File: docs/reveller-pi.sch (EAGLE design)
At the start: 12 parts, among them X1 332-26

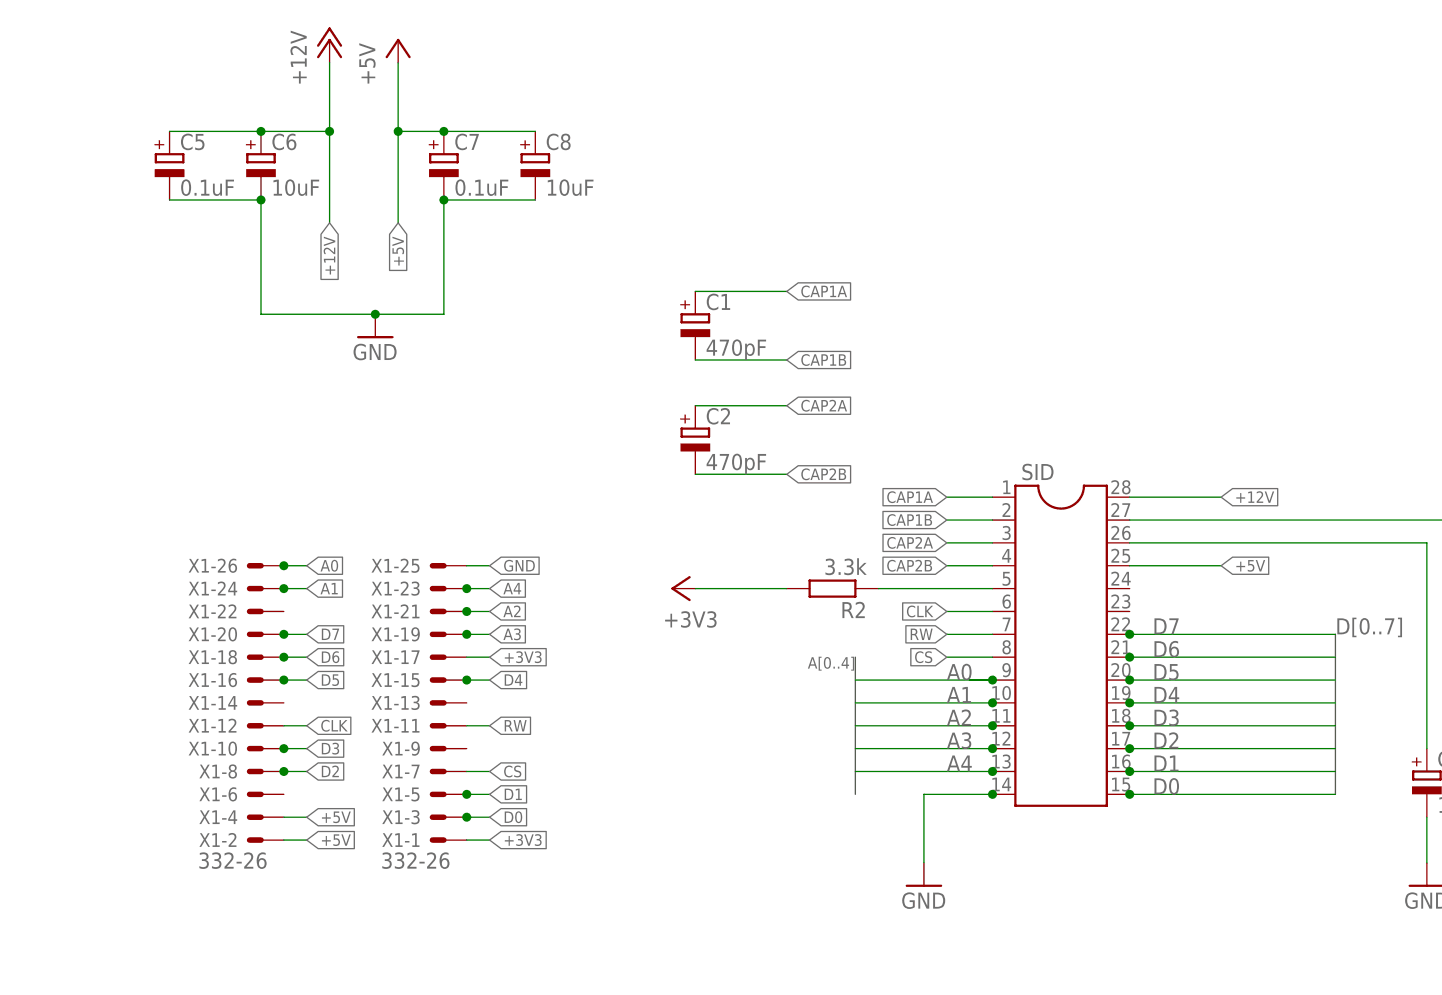
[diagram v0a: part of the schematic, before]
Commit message: updated schematics
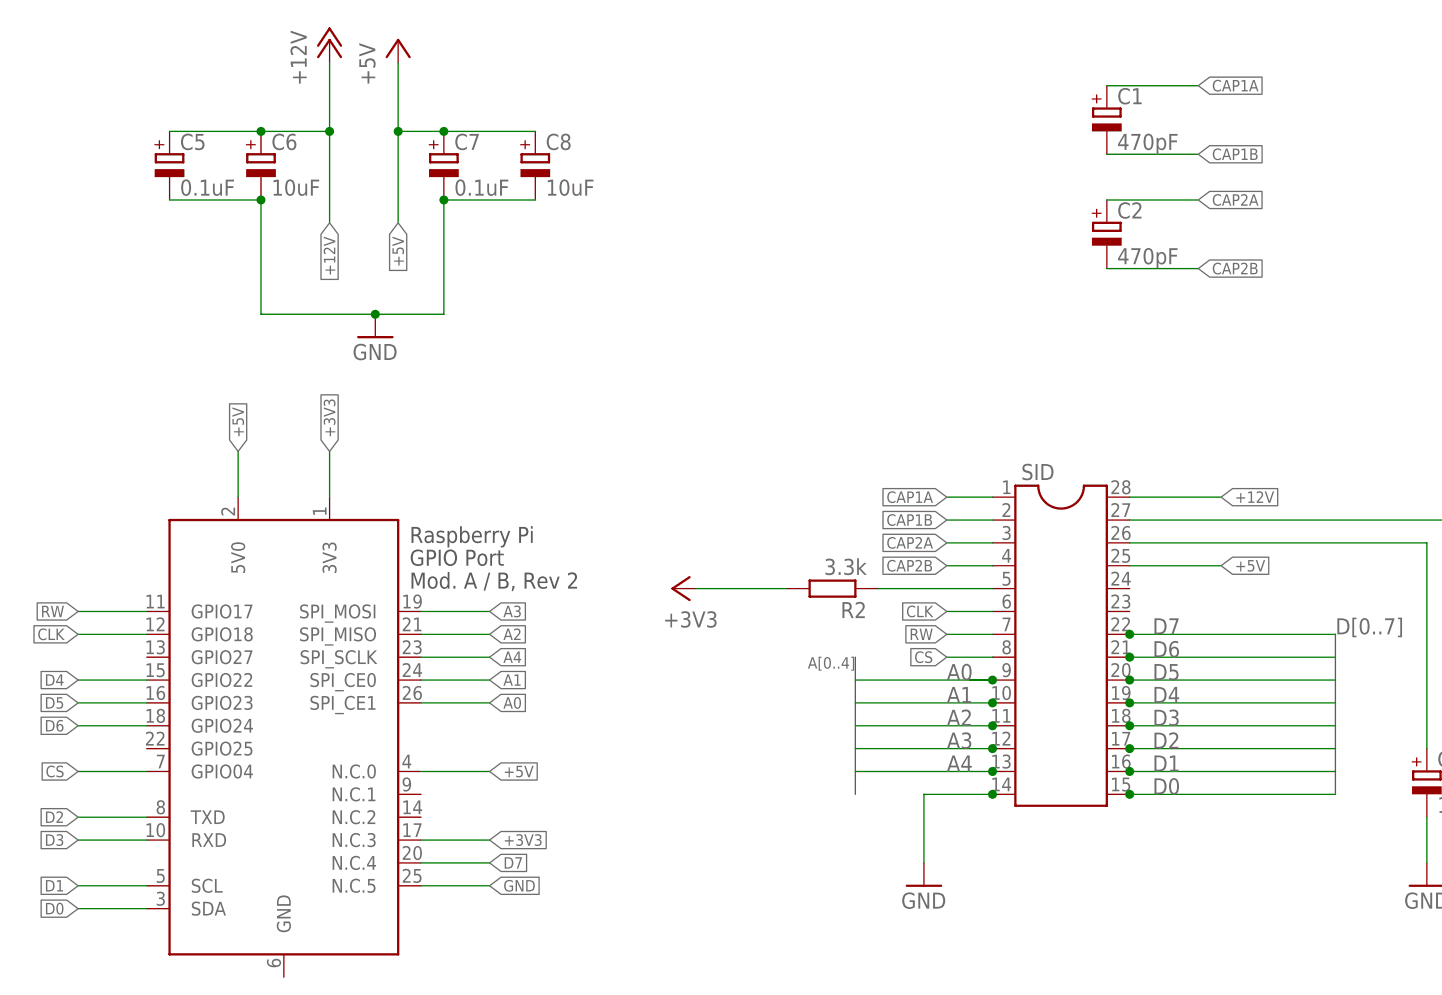
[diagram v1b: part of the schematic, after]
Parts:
- removed X1: 332-26, con-garry:332-26
- added X2: RASPI_BOARD_AB_E0, raspberrypi_bastelstube_v13:RASPI_BOARD_AB_E0
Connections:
- net +3V3: now also X2.3V3, X2.N.C.3; no longer X1-1.S, X1-17.S
- net +5V: now also X2.5V0, X2.N.C.0; no longer X1-2.S, X1-4.S
- net A0: now also X2.SPI_CE1; no longer X1-26.S
- net A1: now also X2.SPI_CE0; no longer X1-24.S
- net A2: now also X2.SPI_MISO; no longer X1-21.S
- net A3: now also X2.SPI_MOSI; no longer X1-19.S
- net A4: now also X2.SPI_SCLK; no longer X1-23.S
- net CLK: now also X2.GPIO18; no longer X1-12.S
- net CS: now also X2.GPIO04; no longer X1-7.S
- net D0: now also X2.SDA; no longer X1-3.S
- net D1: now also X2.SCL; no longer X1-5.S
- net D2: now also X2.TXD; no longer X1-8.S
- net D3: now also X2.RXD; no longer X1-10.S
- net D4: now also X2.GPIO22; no longer X1-15.S
- net D5: now also X2.GPIO23; no longer X1-16.S
- net D6: now also X2.GPIO24; no longer X1-18.S
- net D7: now also X2.N.C.4; no longer X1-20.S
- net GND: now also X2.N.C.5; no longer X1-25.S
- net RW: now also X2.GPIO17; no longer X1-11.S
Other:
- moved on the sheet: C1, C2

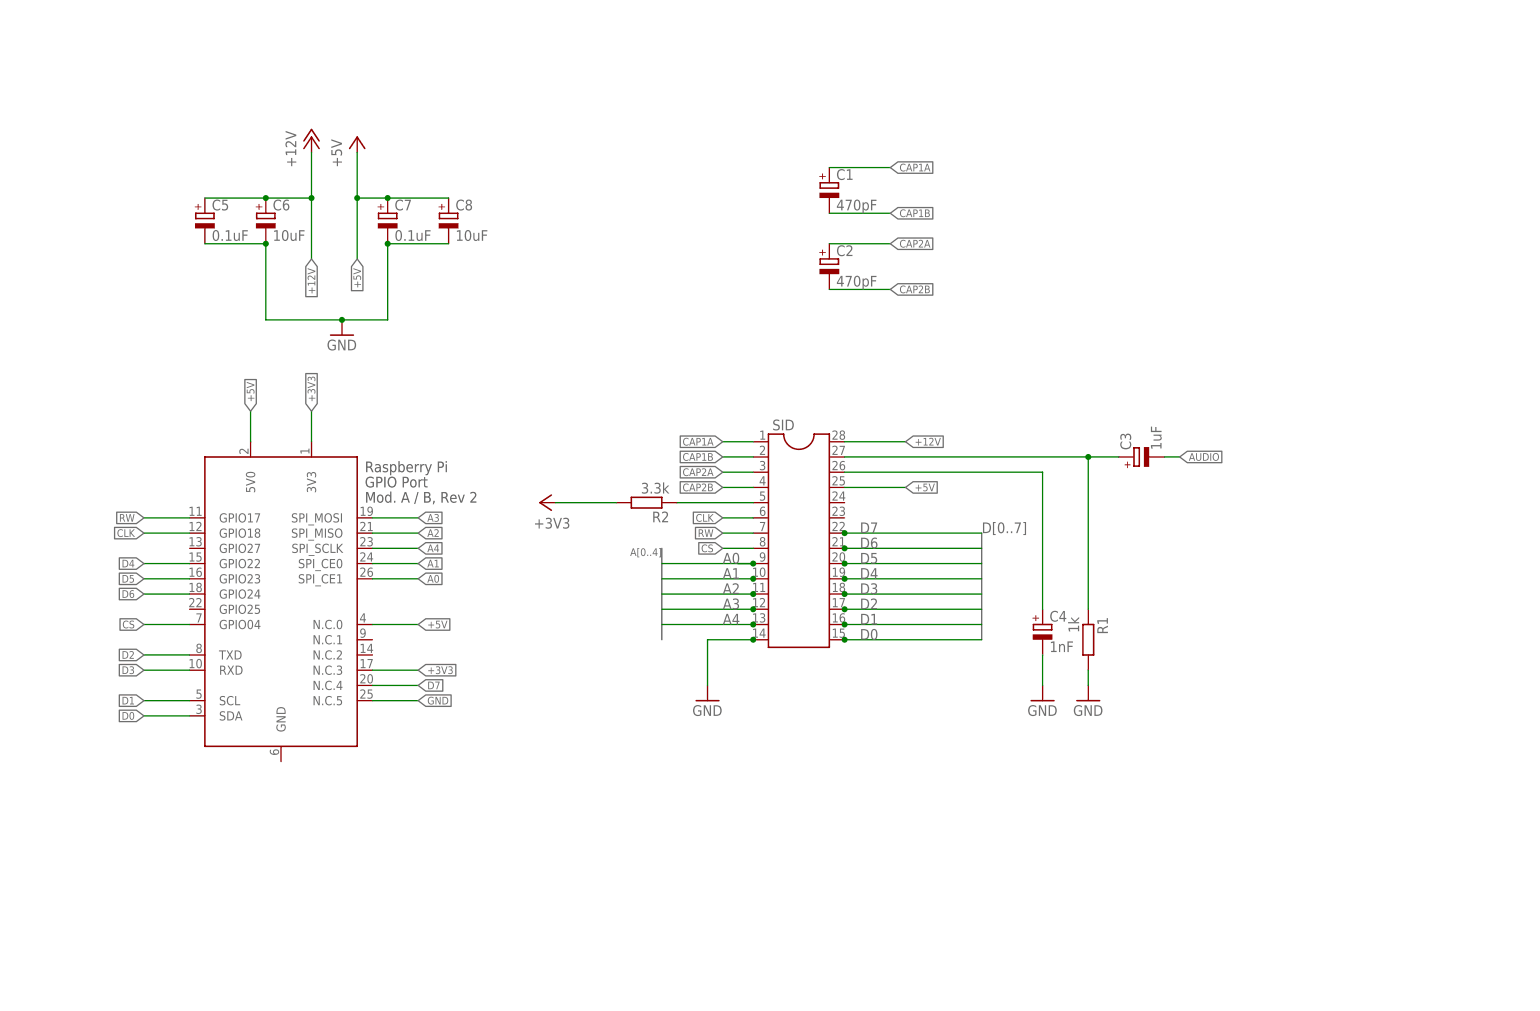
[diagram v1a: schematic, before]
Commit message: updated with mini-audio jack and power control
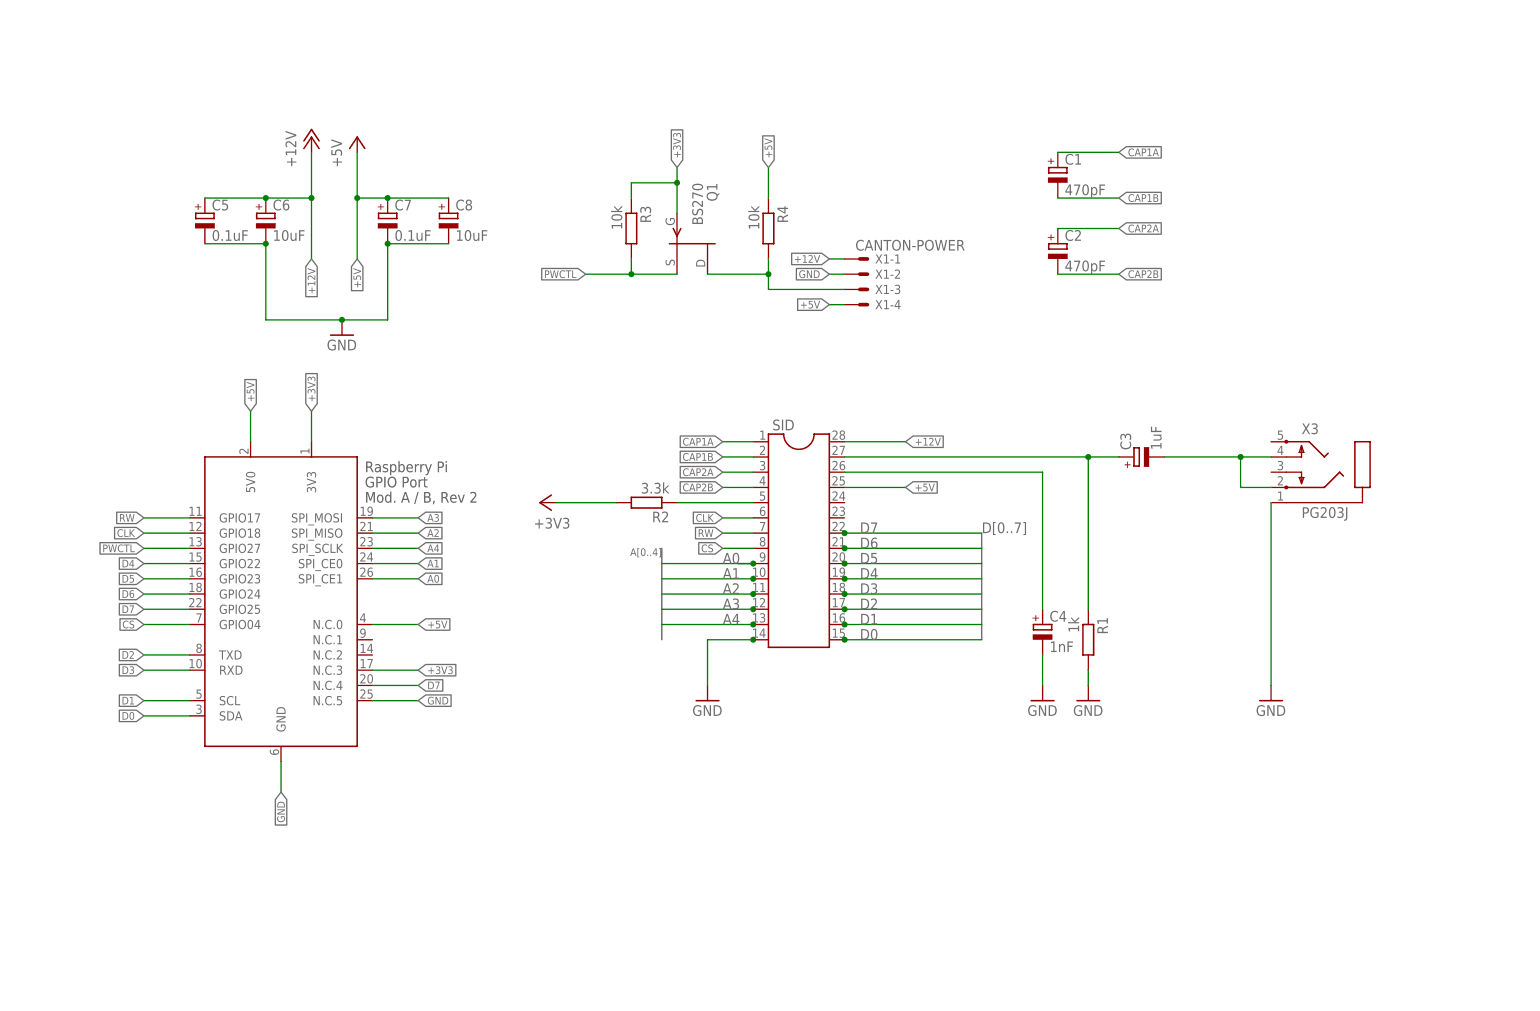
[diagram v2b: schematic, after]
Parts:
- added Q1: BS270, transistor-fet:2N5484
- added R3, R4: 10k, rcl:R-EU_0204/7
- added X1: CANTON-POWER, con-molex:22-23-2041
- added X3: PG203J, con-hirschmann:PG203J
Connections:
- removed net AUDIO: C3.-
- new net N$3: C3.-, X3.2, X3.4
- new net N$4: Q1.D, R4.2, X1-3.S
- new net PWCTL: Q1.S, R3.2, X2.GPIO27
- net +12V: now also X1-1.S
- net +3V3: now also Q1.G, R3.1
- net +5V: now also R4.1, X1-4.S
- net D7: now also X2.GPIO25
- net GND: now also X1-2.S, X2.GND, X3.1
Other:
- moved on the sheet: C1, C2
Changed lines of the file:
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@@
 <layer number="97" name="Info" color="7" fill="1" visible="yes" active="yes"/>
 <layer number="98" name="Guide" color="6" fill="1" visible="yes" active="yes"/>
+<layer number="99" name="SpiceOrder" color="5" fill="1" visible="yes" active="yes"/>
 </layers>
 <schematic xreflabel="%F%N/%S.%C%R" xrefpart="/%S.%C%R">
@@
 <part name="GND4" library="supply1" deviceset="GND" device=""/>
 <part name="X2" library="raspberrypi_bastelstube_v13" deviceset="RASPI_BOARD_AB" device="_E0"/>
+<part name="Q1" library="transistor-fet" deviceset="?548*" device="2N" technology="4" value="BS270"/>
+<part name="R3" library="rcl" deviceset="R-EU_" device="0204/7" value="10k"/>
+<part name="R4" library="rcl" deviceset="R-EU_" device="0204/7" value="10k"/>
+<part name="X1" library="con-molex" deviceset="22-23-2041" device="" value="CANTON-POWER"/>
+<part name="X3" library="con-hirschmann" deviceset="PG203J" device=""/>
+<part name="GND5" library="supply1" deviceset="GND" device=""/>
 </parts>
 <sheets>
@@
 <instance part="P+2" gate="1" x="58.42" y="149.86"/>
 <instance part="GND1" gate="1" x="124.46" y="55.88"/>
-<instance part="C1" gate="G$1" x="144.78" y="142.24"/>
-<instance part="C2" gate="G$1" x="144.78" y="129.54"/>
+<instance part="C1" gate="G$1" x="182.88" y="144.78"/>
+<instance part="C2" gate="G$1" x="182.88" y="132.08"/>
 <instance part="C3" gate="G$1" x="195.58" y="96.52" rot="R90"/>
 <instance part="R2" gate="G$1" x="114.3" y="88.9" rot="R180"/>
@@
 <instance part="GND4" gate="1" x="63.5" y="116.84"/>
 <instance part="X2" gate="G$1" x="53.34" y="71.12"/>
+<instance part="Q1" gate="G$1" x="121.92" y="132.08" rot="R270"/>
+<instance part="R3" gate="G$1" x="111.76" y="134.62" rot="R270"/>
+<instance part="R4" gate="G$1" x="134.62" y="134.62" rot="R270"/>
+<instance part="X1" gate="-1" x="149.86" y="129.54"/>
+<instance part="X1" gate="-2" x="149.86" y="127"/>
+<instance part="X1" gate="-3" x="149.86" y="124.46"/>
+<instance part="X1" gate="-4" x="149.86" y="121.92"/>
+<instance part="X3" gate="1" x="231.14" y="96.52"/>
+<instance part="GND5" gate="1" x="218.44" y="55.88"/>
 </instances>
 <busses>
@@
 <label x="76.2" y="55.88" size="1.27" layer="95" xref="yes"/>
 </segment>
+<segment>
+<pinref part="X1" gate="-2" pin="S"/>
+<wire x1="147.32" y1="127" x2="144.78" y2="127" width="0.1524" layer="91"/>
+<label x="144.78" y="127" size="1.27" layer="95" rot="R180" xref="yes"/>
+</segment>
+<segment>
+<pinref part="X3" gate="1" pin="1"/>
+<pinref part="GND5" gate="1" pin="GND"/>
+<wire x1="218.44" y1="88.9" x2="218.44" y2="58.42" width="0.1524" layer="91"/>
+</segment>
+<segment>
+<pinref part="X2" gate="G$1" pin="GND"/>
+<wire x1="53.34" y1="45.72" x2="53.34" y2="40.64" width="0.1524" layer="91"/>
+<label x="53.34" y="40.64" size="1.27" layer="95" rot="R270" xref="yes"/>
+</segment>
 </net>
 <net name="D0" class="0">
@@
 <label x="76.2" y="58.42" size="1.27" layer="95" xref="yes"/>
 </segment>
+<segment>
+<pinref part="X2" gate="G$1" pin="GPIO25"/>
+<wire x1="38.1" y1="71.12" x2="30.48" y2="71.12" width="0.1524" layer="91"/>
+<label x="30.48" y="71.12" size="1.27" layer="95" rot="R180" xref="yes"/>
+</segment>
 </net>
 <net name="CAP1A" class="0">
 <segment>
 <pinref part="C1" gate="G$1" pin="+"/>
-<wire x1="144.78" y1="144.78" x2="154.94" y2="144.78" width="0.1524" layer="91"/>
-<label x="154.94" y="144.78" size="1.27" layer="95" xref="yes"/>
+<wire x1="182.88" y1="147.32" x2="193.04" y2="147.32" width="0.1524" layer="91"/>
+<label x="193.04" y="147.32" size="1.27" layer="95" xref="yes"/>
 </segment>
 <segment>
@@
 <segment>
 <pinref part="C1" gate="G$1" pin="-"/>
-<wire x1="144.78" y1="137.16" x2="154.94" y2="137.16" width="0.1524" layer="91"/>
-<label x="154.94" y="137.16" size="1.27" layer="95" xref="yes"/>
+<wire x1="182.88" y1="139.7" x2="193.04" y2="139.7" width="0.1524" layer="91"/>
+<label x="193.04" y="139.7" size="1.27" layer="95" xref="yes"/>
 </segment>
 <segment>
@@
 <segment>
 <pinref part="C2" gate="G$1" pin="+"/>
-<wire x1="144.78" y1="132.08" x2="154.94" y2="132.08" width="0.1524" layer="91"/>
-<label x="154.94" y="132.08" size="1.27" layer="95" xref="yes"/>
+<wire x1="182.88" y1="134.62" x2="193.04" y2="134.62" width="0.1524" layer="91"/>
+<label x="193.04" y="134.62" size="1.27" layer="95" xref="yes"/>
 </segment>
 <segment>
@@
 <segment>
 <pinref part="C2" gate="G$1" pin="-"/>
-<wire x1="144.78" y1="124.46" x2="154.94" y2="124.46" width="0.1524" layer="91"/>
-<label x="154.94" y="124.46" size="1.27" layer="95" xref="yes"/>
+<wire x1="182.88" y1="127" x2="193.04" y2="127" width="0.1524" layer="91"/>
+<label x="193.04" y="127" size="1.27" layer="95" xref="yes"/>
 </segment>
 <segment>
@@
 <label x="157.48" y="99.06" size="1.27" layer="95" xref="yes"/>
 </segment>
+<segment>
+<pinref part="X1" gate="-1" pin="S"/>
+<wire x1="147.32" y1="129.54" x2="144.78" y2="129.54" width="0.1524" layer="91"/>
+<label x="144.78" y="129.54" size="1.27" layer="95" rot="R180" xref="yes"/>
+</segment>
 </net>
 <net name="+5V" class="0">
@@
 <label x="48.26" y="104.14" size="1.27" layer="95" rot="R90" xref="yes"/>
 </segment>
+<segment>
+<pinref part="R4" gate="G$1" pin="1"/>
+<wire x1="134.62" y1="139.7" x2="134.62" y2="144.78" width="0.1524" layer="91"/>
+<label x="134.62" y="144.78" size="1.27" layer="95" rot="R90" xref="yes"/>
+</segment>
+<segment>
+<pinref part="X1" gate="-4" pin="S"/>
+<wire x1="147.32" y1="121.92" x2="144.78" y2="121.92" width="0.1524" layer="91"/>
+<label x="144.78" y="121.92" size="1.27" layer="95" rot="R180" xref="yes"/>
+</segment>
 </net>
 <net name="RESET" class="0">
@@
 <wire x1="58.42" y1="99.06" x2="58.42" y2="104.14" width="0.1524" layer="91"/>
 <label x="58.42" y="104.14" size="1.27" layer="95" rot="R90" xref="yes"/>
+</segment>
+<segment>
+<pinref part="Q1" gate="G$1" pin="G"/>
+<wire x1="119.38" y1="137.16" x2="119.38" y2="142.24" width="0.1524" layer="91"/>
+<label x="119.38" y="144.78" size="1.27" layer="95" rot="R90" xref="yes"/>
+<pinref part="R3" gate="G$1" pin="1"/>
+<wire x1="119.38" y1="142.24" x2="119.38" y2="144.78" width="0.1524" layer="91"/>
+<wire x1="111.76" y1="139.7" x2="111.76" y2="142.24" width="0.1524" layer="91"/>
+<wire x1="111.76" y1="142.24" x2="119.38" y2="142.24" width="0.1524" layer="91"/>
+<junction x="119.38" y="142.24"/>
 </segment>
 </net>
@@
 </segment>
 </net>
-<net name="AUDIO" class="0">
+<net name="PWCTL" class="0">
+<segment>
+<pinref part="X2" gate="G$1" pin="GPIO27"/>
+<wire x1="38.1" y1="81.28" x2="30.48" y2="81.28" width="0.1524" layer="91"/>
+<label x="30.48" y="81.28" size="1.27" layer="95" rot="R180" xref="yes"/>
+</segment>
+<segment>
+<pinref part="Q1" gate="G$1" pin="S"/>
+<wire x1="119.38" y1="127" x2="111.76" y2="127" width="0.1524" layer="91"/>
+<label x="104.14" y="127" size="1.27" layer="95" rot="R180" xref="yes"/>
+<pinref part="R3" gate="G$1" pin="2"/>
+<wire x1="111.76" y1="127" x2="104.14" y2="127" width="0.1524" layer="91"/>
+<wire x1="111.76" y1="129.54" x2="111.76" y2="127" width="0.1524" layer="91"/>
+<junction x="111.76" y="127"/>
+</segment>
+</net>
+<net name="N$4" class="0">
+<segment>
+<pinref part="Q1" gate="G$1" pin="D"/>
+<wire x1="124.46" y1="127" x2="134.62" y2="127" width="0.1524" layer="91"/>
+<pinref part="R4" gate="G$1" pin="2"/>
+<wire x1="134.62" y1="129.54" x2="134.62" y2="127" width="0.1524" layer="91"/>
+<wire x1="134.62" y1="127" x2="134.62" y2="124.46" width="0.1524" layer="91"/>
+<junction x="134.62" y="127"/>
+<pinref part="X1" gate="-3" pin="S"/>
+<wire x1="134.62" y1="124.46" x2="147.32" y2="124.46" width="0.1524" layer="91"/>
+</segment>
+</net>
+<net name="N$3" class="0">
 <segment>
 <pinref part="C3" gate="G$1" pin="-"/>
-<wire x1="200.66" y1="96.52" x2="203.2" y2="96.52" width="0.1524" layer="91"/>
-<label x="203.2" y="96.52" size="1.27" layer="95" xref="yes"/>
-</segment>
-</net>
+<pinref part="X3" gate="1" pin="4"/>
+<wire x1="200.66" y1="96.52" x2="213.36" y2="96.52" width="0.1524" layer="91"/>
+<pinref part="X3" gate="1" pin="2"/>
+<wire x1="213.36" y1="96.52" x2="218.44" y2="96.52" width="0.1524" layer="91"/>
+<wire x1="218.44" y1="91.44" x2="213.36" y2="91.44" width="0.1524" layer="91"/>
+<wire x1="213.36" y1="91.44" x2="213.36" y2="96.52" width="0.1524" layer="91"/>
+<junction x="213.36" y="96.52"/>
+</segment>
+</net>
